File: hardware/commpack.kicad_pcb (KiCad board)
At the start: 2 copper layers, 103.8 x 62.5 mm, 12 parts, among them J1 1240COMM, J2 1240COMM_EXT

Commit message: Rename project files to remove LXI mark.
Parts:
- Bonsai: footprint 1240comm:Bonsai -> ether1240:Bonsai
- G***: footprint 1240comm:OSHW -> ether1240:OSHW
- H1, H2, H3, H4: footprint 1240comm:MountingHole_140mil_Pad -> ether1240:MountingHole_140mil_Pad
- J2: footprint 1240comm:ATA_HEADER -> ether1240:ATA_HEADER
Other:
- board text added: "Ethernet Comm Pack for Tektronix 1240 v0.1 © 2017 Sam Hanes <sam@maltera.com> Licensed under CERN OHL v1.2 or newer https://github.com/Elemecca/ether1240"
- board text removed: "LXI Comm Pack for Tektronix 1240 v0.1 © 2017 Sam Hanes <sam@maltera.com> Licensed under CERN OHL v1.2 or newer https://github.com/Elemecca/lxi1240"
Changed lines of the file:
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@@
   (page A4)
   (title_block
-    (title "LXI Comm Pack for Tektronix 1240")
+    (title "Ethernet Comm Pack for Tektronix 1240")
     (company "© 2017 Sam Hanes <sam@maltera.com>")
     (comment 1 "Licensed under CERN OHL v1.2 or newer")
-    (comment 2 https://github.com/Elemecca/lxi1240)
+    (comment 2 https://github.com/Elemecca/ether1240)
   )
   (layers
@@
     (add_net GND)
   )
-  (module 1240comm:ATA_HEADER (layer F.Cu)
+  (module ether1240:ATA_HEADER (layer F.Cu)
     (at 201.295 64.77)
     (descr "Through hole straight pin header, 2x20, 2.54mm pitch, double rows")
@@
       (solder_mask_margin 0.5) (clearance 0.5))
   )
-  (module 1240comm:OSHW (layer B.Cu)
+  (module ether1240:OSHW (layer B.Cu)
     (at 171.45 81.28 180)
     (fp_text reference G*** (at 0 -6.73608 180) (layer B.SilkS) hide
@@
       (xy 3.85064 -5.70484)) (layer B.SilkS) (width 0.00254))
   )
-  (module 1240comm:Bonsai (layer F.Cu)
+  (module ether1240:Bonsai (layer F.Cu)
     (at 184.15 81.915)
     (descr "Imported from Bonsai.svg")
@@
       (xy -5.997155 -3.032912) (xy -5.955922 -3.09889)) (layer B.SilkS) (width 0))
   )
-  (module 1240comm:MountingHole_140mil_Pad (layer F.Cu)
+  (module ether1240:MountingHole_140mil_Pad (layer F.Cu)
     (at 210.82 113.665)
     (descr "Mounting Hole 140mil")
@@
       (net 3 Earth_Protective))
   )
-  (module 1240comm:MountingHole_140mil_Pad (layer F.Cu)
+  (module ether1240:MountingHole_140mil_Pad (layer F.Cu)
     (at 125.73 113.665)
     (descr "Mounting Hole 140mil")
@@
       (net 3 Earth_Protective))
   )
-  (module 1240comm:MountingHole_140mil_Pad (layer F.Cu)
+  (module ether1240:MountingHole_140mil_Pad (layer F.Cu)
     (at 125.73 64.135)
     (descr "Mounting Hole 140mil")
@@
       (net 3 Earth_Protective))
   )
-  (module 1240comm:MountingHole_140mil_Pad (layer F.Cu)
+  (module ether1240:MountingHole_140mil_Pad (layer F.Cu)
     (at 210.82 64.135)
     (descr "Mounting Hole 140mil")
@@
   (gr_line (start 214.63 62.23) (end 214.249 62.23) (layer Edge.Cuts) (width 0.15))
   (gr_line (start 214.249 62.23) (end 214.249 60.198) (layer Edge.Cuts) (width 0.15))
-  (gr_text "LXI Comm Pack for Tektronix 1240 v0.1\n© 2017 Sam Hanes <sam@maltera.com>\nLicensed under CERN OHL v1.2 or newer\nhttps://github.com/Elemecca/lxi1240" (at 190.5 68.58) (layer B.SilkS)
+  (gr_text "Ethernet Comm Pack for Tektronix 1240 v0.1\n© 2017 Sam Hanes <sam@maltera.com>\nLicensed under CERN OHL v1.2 or newer\nhttps://github.com/Elemecca/ether1240" (at 190.5 68.58) (layer B.SilkS)
     (effects (font (size 1.5 1.5) (thickness 0.3)) (justify left mirror))
   )

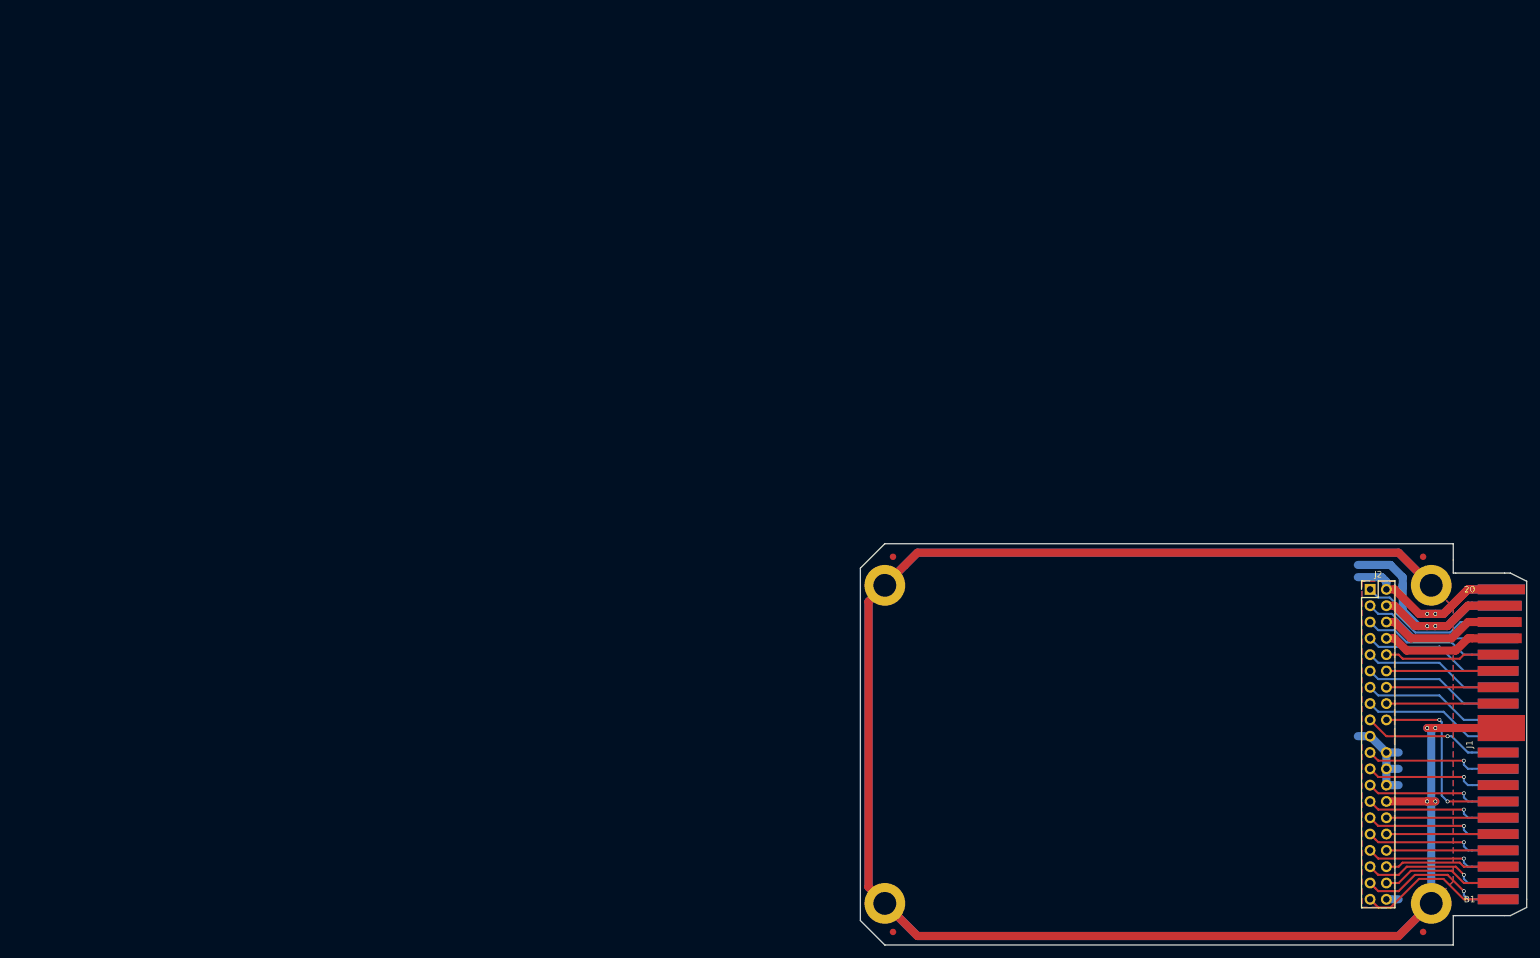
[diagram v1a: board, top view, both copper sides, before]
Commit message: Build footprint for MagJack.
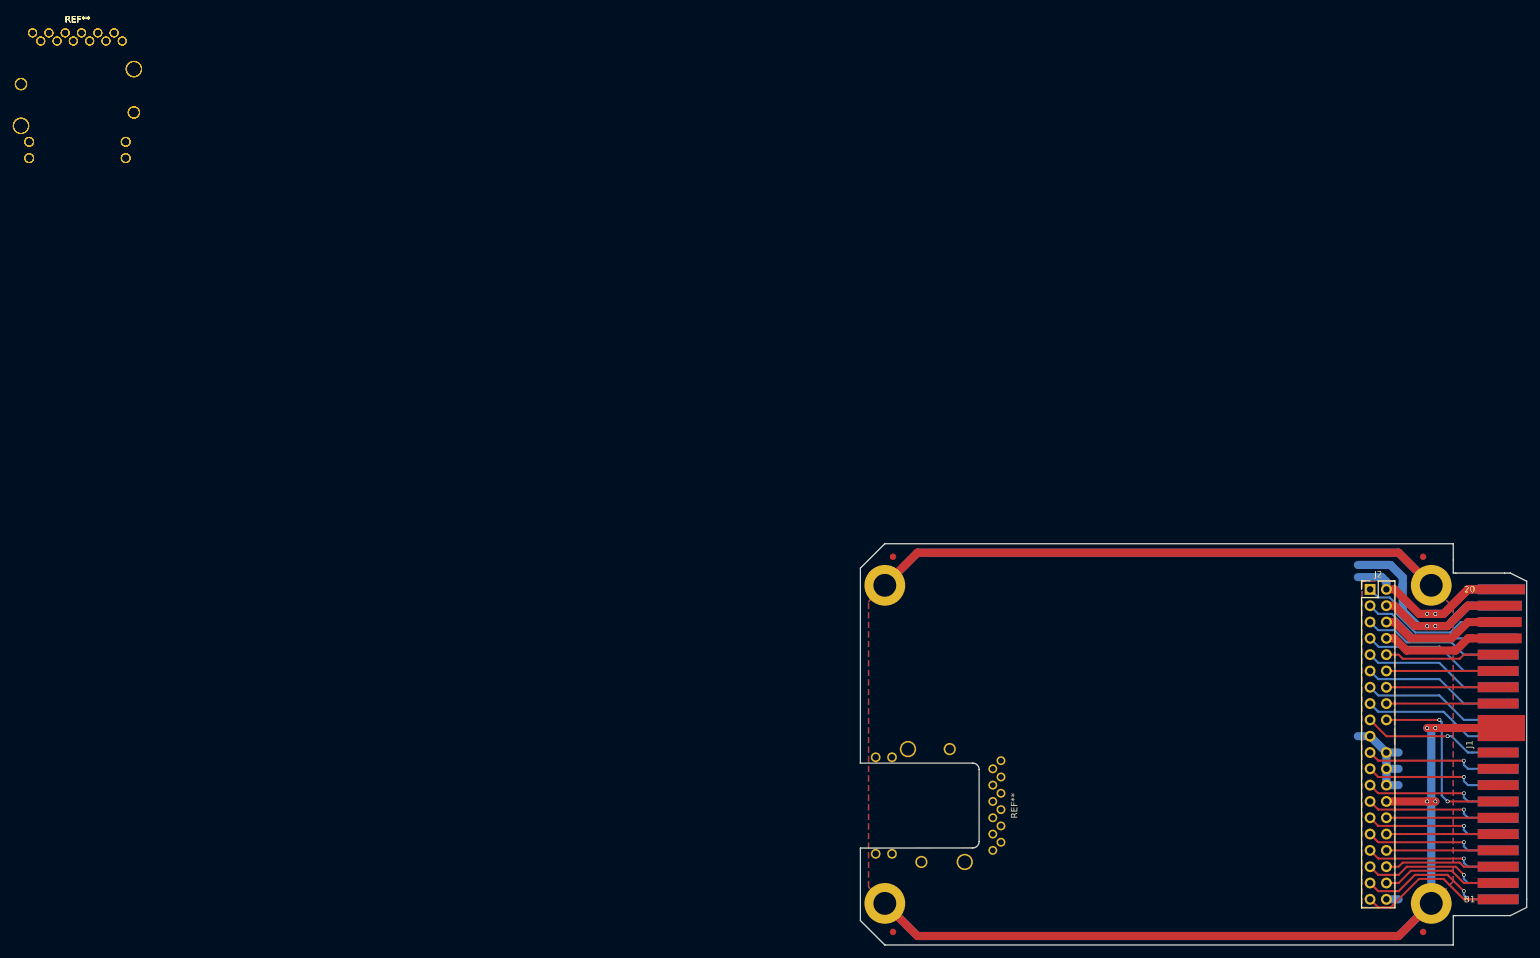
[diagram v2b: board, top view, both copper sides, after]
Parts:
- added REF**: L8BE-1G1T-91A, ether1240:L8BE-1G1T-91A, F.Cu at (0.00, 0.00)
- added REF** (x2): L8BE-1G1T-91A, L8BE-1G1T-91A, F.Cu at (0.00, 0.00)
- added REF**: L8BE-1G1T-91A, ether1240:L8BE-1G1T-91A, F.Cu at (121.9, 98.4)
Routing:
- net Earth_Protective: track 506.4 -> 403.2 mm
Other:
- outline, holes or cut-outs redrawn

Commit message: Remove PIC16, add Ethernet port to schematic, fix SGND.
The PIC16 micro isn't fast enough to perform reliable bus emulation.
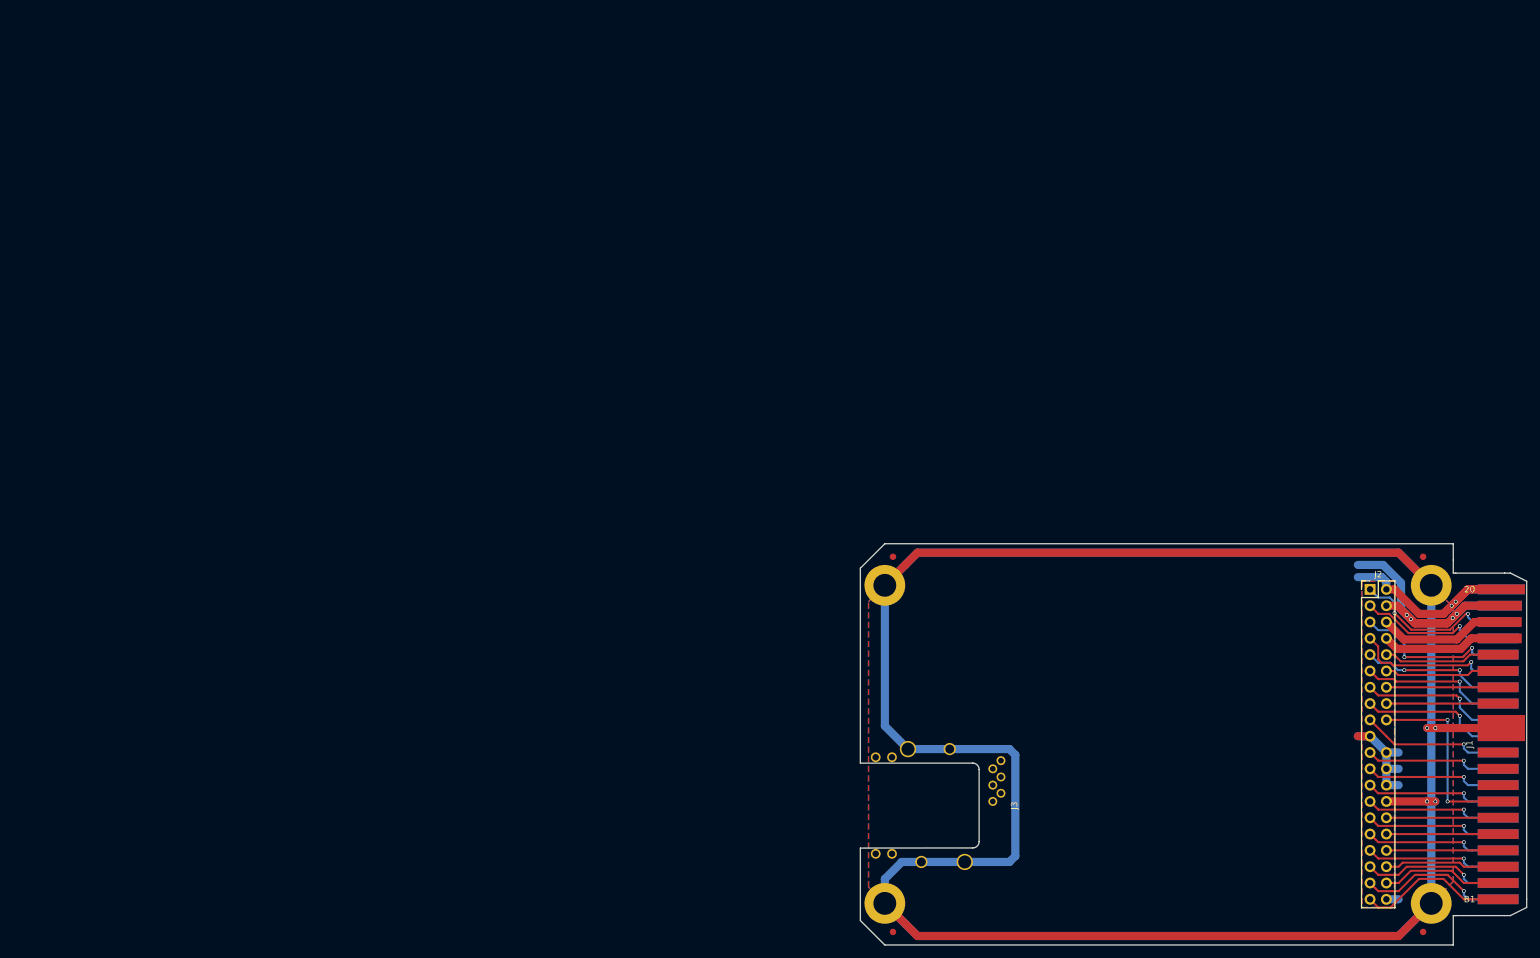
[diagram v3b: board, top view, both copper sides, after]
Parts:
- removed REF**: L8BE-1G1T-91A, ether1240:L8BE-1G1T-91A
- removed REF** (x2): L8BE-1G1T-91A, L8BE-1G1T-91A
- J3: renamed from REF**; footprint ether1240:L8BE-1G1T-91A -> L8BE-1G1T-91A
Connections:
- net /~H-CS renamed /H-~CS
- net /~H-RD renamed /H-~RD
- net /~H-RS renamed /H-~RS
- net /~H-WR renamed /H-~WR
- J3 pad 10: (no net) -> Net-(J3-Pad10)
- J3 pad 11: (no net) -> Net-(J3-Pad11)
- J3 pad 12: (no net) -> Net-(J3-Pad12)
- J3 pad 13: (no net) -> Net-(J3-Pad13)
- J3 pad 14: (no net) -> Net-(J3-Pad14)
- J3 pad 15: (no net) -> Net-(J3-Pad15)
- J3 pad 16: (no net) -> Net-(J3-Pad16)
- J3 pad 4: (no net) -> Net-(J3-Pad4)
- J3 pad 5: (no net) -> Net-(J3-Pad5)
- J3 pad 6: (no net) -> Net-(J3-Pad6)
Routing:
- net Earth_Protective: track 403.2 -> 510.8 mm
- net +5V: track 47.8 -> 41.3 mm, vias 2 -> 4
- net /H-A0: track 18.9 -> 21.9 mm, vias 0 -> 2
- net GND: track 54.6 -> 52.1 mm
- net /H-~RD: track 18.9 -> 21.1 mm, vias 0 -> 1
- net /H-A2: track 18.9 -> 20.1 mm, vias 0 -> 1
- net /H-A4: track 21.1 -> 22.2 mm, vias 0 -> 2
- net /H-~RS: track 18.9 -> 19.8 mm, vias 0 -> 1
- net Net-(J1-PadA12): track 18.9 -> 19.7 mm, vias 0 -> 1
- net /H-A13: track 26.2 -> 26.9 mm
- net /H-D0: track 18.9 -> 19.6 mm, vias 0 -> 1
- net /H-INT: track 18.9 -> 19.4 mm, vias 0 -> 2
- net /H-A8: track 14.2 -> 14.8 mm

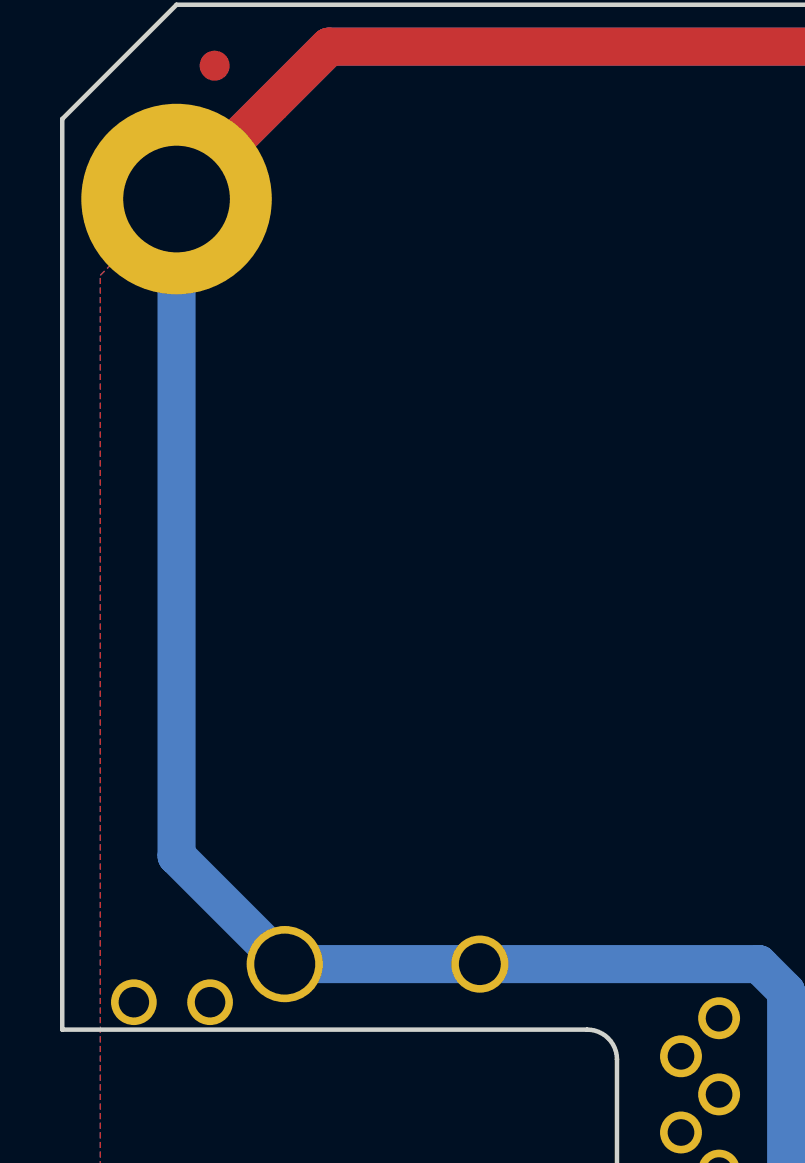
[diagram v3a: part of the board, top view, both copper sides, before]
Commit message: Add USB-B connector.
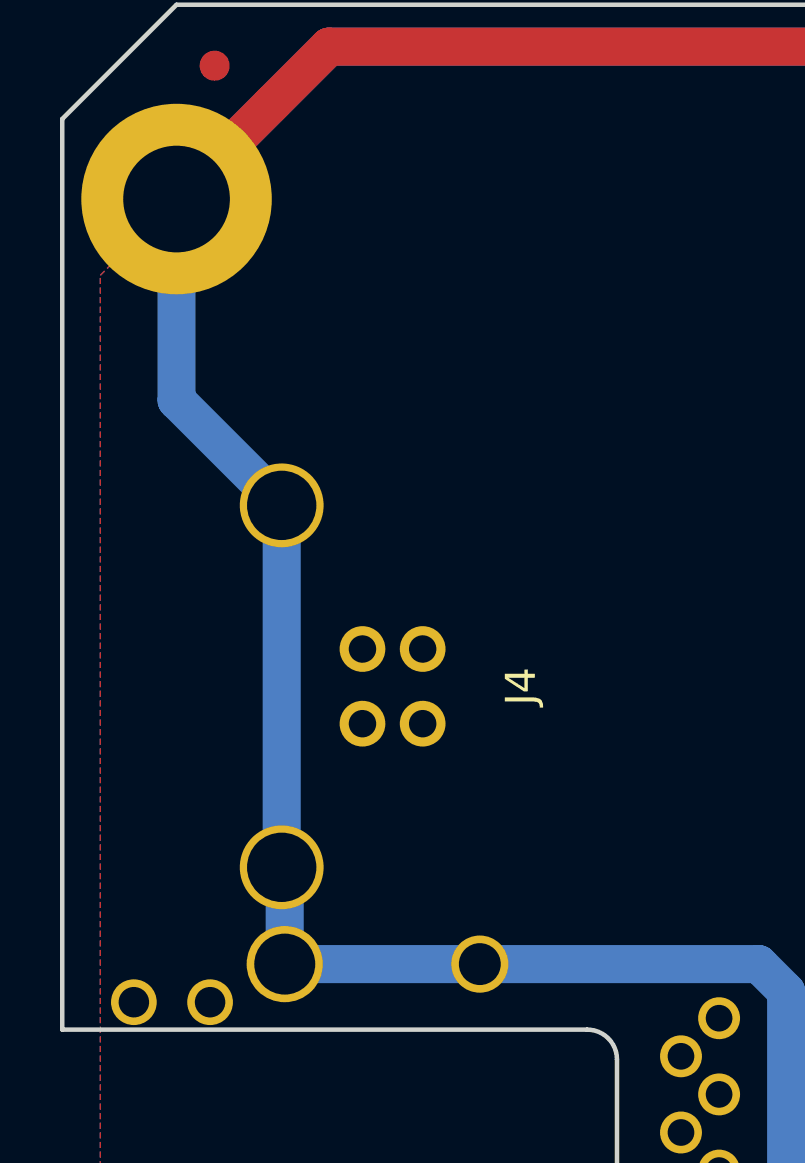
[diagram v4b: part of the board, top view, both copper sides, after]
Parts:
- added J4: USB_B, USB-B, F.Cu at (121.9, 80.4)
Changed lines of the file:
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@@
 (kicad_pcb (version 4) (host pcbnew 4.0.7)
   (general
-    (links 49)
+    (links 52)
     (no_connects 0)
     (area 121.844999 57.582999 225.754001 120.217001)
     (thickness 1.6)
     (drawings 66)
-    (tracks 299)
+    (tracks 302)
     (zones 0)
-    (modules 13)
-    (nets 48)
+    (modules 14)
+    (nets 51)
   )
   (page A4)
@@
   (net 46 "Net-(J3-Pad5)")
   (net 47 "Net-(J3-Pad4)")
+  (net 48 "Net-(J4-Pad3)")
+  (net 49 "Net-(J4-Pad2)")
+  (net 50 "Net-(J4-Pad1)")
   (net_class Default "This is the default net class."
     (clearance 0.2)
@@
     (add_net "Net-(J3-Pad5)")
     (add_net "Net-(J3-Pad6)")
+    (add_net "Net-(J4-Pad1)")
+    (add_net "Net-(J4-Pad2)")
+    (add_net "Net-(J4-Pad3)")
   )
   (net_class Power ""
@@
     (add_net Earth_Protective)
     (add_net GND)
+  )
+  (module USB-B (layer F.Cu)
+    (at 121.92 80.3783 270)
+    (fp_text reference J4 (at 0 -15.2908 270) (layer F.SilkS)
+      (effects (font (size 1 1) (thickness 0.15)))
+    )
+    (fp_text value USB_B (at 0 0.9652 270) (layer F.Fab)
+      (effects (font (size 1 1) (thickness 0.15)))
+    )
+    (fp_line (start -5.9944 0) (end 5.9944 0) (layer F.Fab) (width 0.15))
+    (fp_line (start -7.366 -14.5288) (end -7.366 -13.7668) (layer F.CrtYd) (width 0.15))
+    (fp_line (start 7.366 -14.5288) (end -7.366 -14.5288) (layer F.CrtYd) (width 0.15))
+    (fp_line (start 7.366 -13.7668) (end 7.366 -14.5288) (layer F.CrtYd) (width 0.15))
+    (fp_line (start 7.366 -13.7668) (end 7.366 2.9972) (layer F.CrtYd) (width 0.15))
+    (fp_line (start -7.366 -13.5128) (end -7.366 -13.7668) (layer F.CrtYd) (width 0.15))
+    (fp_line (start -7.366 2.9972) (end -7.366 -13.5128) (layer F.CrtYd) (width 0.15))
+    (fp_line (start -7.3152 2.9972) (end -7.366 2.9972) (layer F.CrtYd) (width 0.15))
+    (fp_line (start 7.366 2.9972) (end -7.3152 2.9972) (layer F.CrtYd) (width 0.15))
+    (fp_line (start -5.9944 -13.2588) (end 5.9944 -13.2588) (layer F.Fab) (width 0.15))
+    (fp_line (start -5.9944 2.9972) (end -5.9944 -13.2588) (layer F.Fab) (width 0.15))
+    (fp_line (start 5.9944 2.9972) (end 5.9944 -13.2588) (layer F.Fab) (width 0.15))
+    (fp_line (start 5.9944 2.9972) (end -5.9944 2.9972) (layer F.Fab) (width 0.15))
+    (pad 5 thru_hole circle (at -6.0325 -7.3152 270) (size 2.794 2.794) (drill 2.3114) (layers *.Cu *.Mask)
+      (net 3 Earth_Protective))
+    (pad 5 thru_hole circle (at 6.0325 -7.3152 270) (size 2.794 2.794) (drill 2.3114) (layers *.Cu *.Mask)
+      (net 3 Earth_Protective))
+    (pad 4 thru_hole circle (at 1.2446 -10.0076 270) (size 1.524 1.524) (drill 0.9144) (layers *.Cu *.Mask)
+      (net 1 GND))
+    (pad 3 thru_hole circle (at -1.2446 -10.0076 270) (size 1.524 1.524) (drill 0.9144) (layers *.Cu *.Mask)
+      (net 48 "Net-(J4-Pad3)"))
+    (pad 2 thru_hole circle (at -1.2446 -12.0142 270) (size 1.524 1.524) (drill 0.9144) (layers *.Cu *.Mask)
+      (net 49 "Net-(J4-Pad2)"))
+    (pad 1 thru_hole circle (at 1.2446 -12.0142 270) (size 1.524 1.524) (drill 0.9144) (layers *.Cu *.Mask)
+      (net 50 "Net-(J4-Pad1)"))
   )
   (module ether1240:ATA_HEADER (layer F.Cu)
@@
   (segment (start 218.059 67.31) (end 216.073908 67.31) (width 1.27) (layer F.Cu) (net 2))
   (segment (start 213.333898 70.05001) (end 208.306101 70.050009) (width 1.27) (layer F.Cu) (net 2))
+  (segment (start 125.73 64.135) (end 125.73 70.8406) (width 1.27) (layer B.Cu) (net 3))
+  (segment (start 125.73 70.8406) (end 129.2352 74.3458) (width 1.27) (layer B.Cu) (net 3))
+  (segment (start 129.2352 86.4108) (end 129.2352 74.3458) (width 1.27) (layer B.Cu) (net 3))
+  (segment (start 129.3368 89.6366) (end 129.3368 86.5124) (width 1.27) (layer B.Cu) (net 3))
+  (segment (start 129.3368 86.5124) (end 129.2352 86.4108) (width 1.27) (layer B.Cu) (net 3))
   (segment (start 125.73 113.665) (end 125.73 109.855) (width 1.27) (layer B.Cu) (net 3))
   (segment (start 125.73 109.855) (end 128.3716 107.2134) (width 1.27) (layer B.Cu) (net 3))
@@
   (segment (start 145.1356 107.2134) (end 138.176 107.2134) (width 1.27) (layer B.Cu) (net 3))
   (segment (start 129.3368 89.6366) (end 135.8392 89.6366) (width 1.27) (layer B.Cu) (net 3))
-  (segment (start 125.73 64.135) (end 125.73 86.0298) (width 1.27) (layer B.Cu) (net 3))
-  (segment (start 125.73 86.0298) (end 129.3368 89.6366) (width 1.27) (layer B.Cu) (net 3))
   (segment (start 210.82 86.36) (end 210.82 64.135) (width 1.27) (layer B.Cu) (net 3))
   (segment (start 203.835 97.79) (end 210.185 97.79) (width 1.27) (layer F.Cu) (net 3))
